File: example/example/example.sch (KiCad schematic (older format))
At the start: 9 parts, among them U1 ATMEGA32U4

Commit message: Kicad template 4x12
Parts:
- removed U1: ATMEGA32U4, mx:Pro_Micro, symbol mx:ATMEGA32U4
- added D10, D11, D12, D15, D16, D17, D18, D19, D20, D21, D22, D23, D24, D25, D26, D27, D28, D29, D3, D30, D31, D32, D33, D34, D35, D36, D37, D38, D39, D4, D40, D41, D42, D43, D44, D45, D46, D47, D48, D5, D6, D7, D8, D9: D, Diode_THT:D_DO-35_SOD27_P7.62mm_Horizontal, symbol Device:D
- added K10, K11, K12, K15, K16, K17, K18, K19, K20, K21, K22, K23, K24, K25, K26, K27, K28, K29, K3, K30, K31, K32, K33, K34, K35, K36, K37, K38, K39, K4, K40, K41, K42, K43, K44, K45, K46, K47, K48, K5, K6, K7, K8, K9: KEYSW, Button_Switch_Keyboard:SW_Cherry_MX_1.00u_Plate, symbol example-rescue:KEYSW-mx
- added SW1: SW_Push, Button_Switch_THT:SW_PUSH_6mm_H5mm, symbol Switch:SW_Push
- added U1: ProMicro, localib:pro_micro, symbol ProMicro:ProMicro
- D1: renamed from D2; footprint Diode_THT:D_DO-15_P10.16mm_Horizontal -> Diode_THT:D_DO-35_SOD27_P7.62mm_Horizontal
- D13: renamed from D1; footprint Diode_THT:D_DO-15_P10.16mm_Horizontal -> Diode_THT:D_DO-35_SOD27_P7.62mm_Horizontal
- D14: renamed from D4; footprint Diode_THT:D_DO-15_P10.16mm_Horizontal -> Diode_THT:D_DO-35_SOD27_P7.62mm_Horizontal
- D2: renamed from D3; footprint Diode_THT:D_DO-15_P10.16mm_Horizontal -> Diode_THT:D_DO-35_SOD27_P7.62mm_Horizontal
- K1: renamed from K?2; footprint Button_Switch_Keyboard:SW_Cherry_MX_1.00u_PCB -> Button_Switch_Keyboard:SW_Cherry_MX_1.00u_Plate; symbol mx:KEYSW -> example-rescue:KEYSW-mx
- K13: renamed from K?1; footprint Button_Switch_Keyboard:SW_Cherry_MX_1.00u_PCB -> Button_Switch_Keyboard:SW_Cherry_MX_1.00u_Plate; symbol mx:KEYSW -> example-rescue:KEYSW-mx
- K14: renamed from K?4; footprint Button_Switch_Keyboard:SW_Cherry_MX_1.00u_PCB -> Button_Switch_Keyboard:SW_Cherry_MX_1.00u_Plate; symbol mx:KEYSW -> example-rescue:KEYSW-mx
- K2: renamed from K?3; footprint Button_Switch_Keyboard:SW_Cherry_MX_1.00u_PCB -> Button_Switch_Keyboard:SW_Cherry_MX_1.00u_Plate; symbol mx:KEYSW -> example-rescue:KEYSW-mx
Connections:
- net +5V: now also U1.21 (5V)
- net col0: now also K25.1, K37.1, U1.20 (21)
- net col1: now also K26.1, K38.1, U1.19 (20)
- net row0: now also D1.1 (K), D2.1 (K), D10.1 (K), D11.1 (K), D12.1 (K), D3.1 (K), D4.1 (K), D5.1 (K), D6.1 (K), D7.1 (K), D8.1 (K), D9.1 (K), U1.18 (19)
- net row1: now also D13.1 (K), D14.1 (K), D15.1 (K), D16.1 (K), D17.1 (K), D18.1 (K), D19.1 (K), D20.1 (K), D21.1 (K), D22.1 (K), D23.1 (K), D24.1 (K), U1.15 (14)
- new net: SW1.1, U1.22 (RST)
- new net: D25.2 (A), K25.2
- new net: D37.2 (A), K37.2
- new net: D26.2 (A), K26.2
- new net: D38.2 (A), K38.2
- new net: D3.2 (A), K3.2
- new net: D4.2 (A), K4.2
- new net: D5.2 (A), K5.2
- new net: D6.2 (A), K6.2
- new net: D7.2 (A), K7.2
- new net: D8.2 (A), K8.2
- new net: D9.2 (A), K9.2
- new net: D10.2 (A), K10.2
- new net: D11.2 (A), K11.2
- new net: D27.2 (A), K27.2
- new net: D39.2 (A), K39.2
- new net: D16.2 (A), K16.2
- new net: D12.2 (A), K12.2
- new net: D28.2 (A), K28.2
- new net: D40.2 (A), K40.2
- new net: D29.2 (A), K29.2
- new net: D17.2 (A), K17.2
- new net: D41.2 (A), K41.2
- new net: D18.2 (A), K18.2
- new net: D19.2 (A), K19.2
- new net: D20.2 (A), K20.2
- new net: D21.2 (A), K21.2
- new net: D22.2 (A), K22.2
- new net: D23.2 (A), K23.2
- new net: D24.2 (A), K24.2
- new net: D30.2 (A), K30.2
- new net: D31.2 (A), K31.2
- new net: D32.2 (A), K32.2
- new net: D33.2 (A), K33.2
- new net: D34.2 (A), K34.2
- new net: D35.2 (A), K35.2
- new net: D36.2 (A), K36.2
- new net: D42.2 (A), K42.2
- new net: D43.2 (A), K43.2
- new net: D44.2 (A), K44.2
- new net: D45.2 (A), K45.2
- new net: D46.2 (A), K46.2
- new net: D47.2 (A), K47.2
- new net: D48.2 (A), K48.2
- new net GND: SW1.2, U1.23 (GND), U1.3 (GND), U1.4 (GND)
- new net col10: K11.1, K23.1, K35.1, K47.1, U1.2 (0)
- new net col11: K12.1, K24.1, K36.1, K48.1, U1.1
- new net col2: K15.1, K27.1, K3.1, K39.1, U1.12 (9)
- new net col3: K16.1, K28.1, K4.1, K40.1, U1.11 (8)
- new net col4: K17.1, K29.1, K41.1, K5.1, U1.10 (7)
- new net col5: K18.1, K30.1, K42.1, K6.1, U1.9 (6)
- new net col6: K19.1, K31.1, K43.1, K7.1, U1.8 (5)
- new net col7: K20.1, K32.1, K44.1, K8.1, U1.7 (4)
- new net col8: K21.1, K33.1, K45.1, K9.1, U1.6 (3)
- new net col9: K10.1, K22.1, K34.1, K46.1, U1.5 (2)
- new net pin15: U1.16 (15)
- new net pin18: U1.17 (18)
- new net row2: D25.1 (K), D26.1 (K), D27.1 (K), D28.1 (K), D29.1 (K), D30.1 (K), D31.1 (K), D32.1 (K), D33.1 (K), D34.1 (K), D35.1 (K), D36.1 (K), U1.14 (16)
- new net row3: D37.1 (K), D38.1 (K), D39.1 (K), D40.1 (K), D41.1 (K), D42.1 (K), D43.1 (K), D44.1 (K), D45.1 (K), D46.1 (K), D47.1 (K), D48.1 (K), U1.13 (10)
- no-connect marks 38 -> 1
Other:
- moved on the sheet: D1, D13, D14, D2, K1, K13, K14, K2

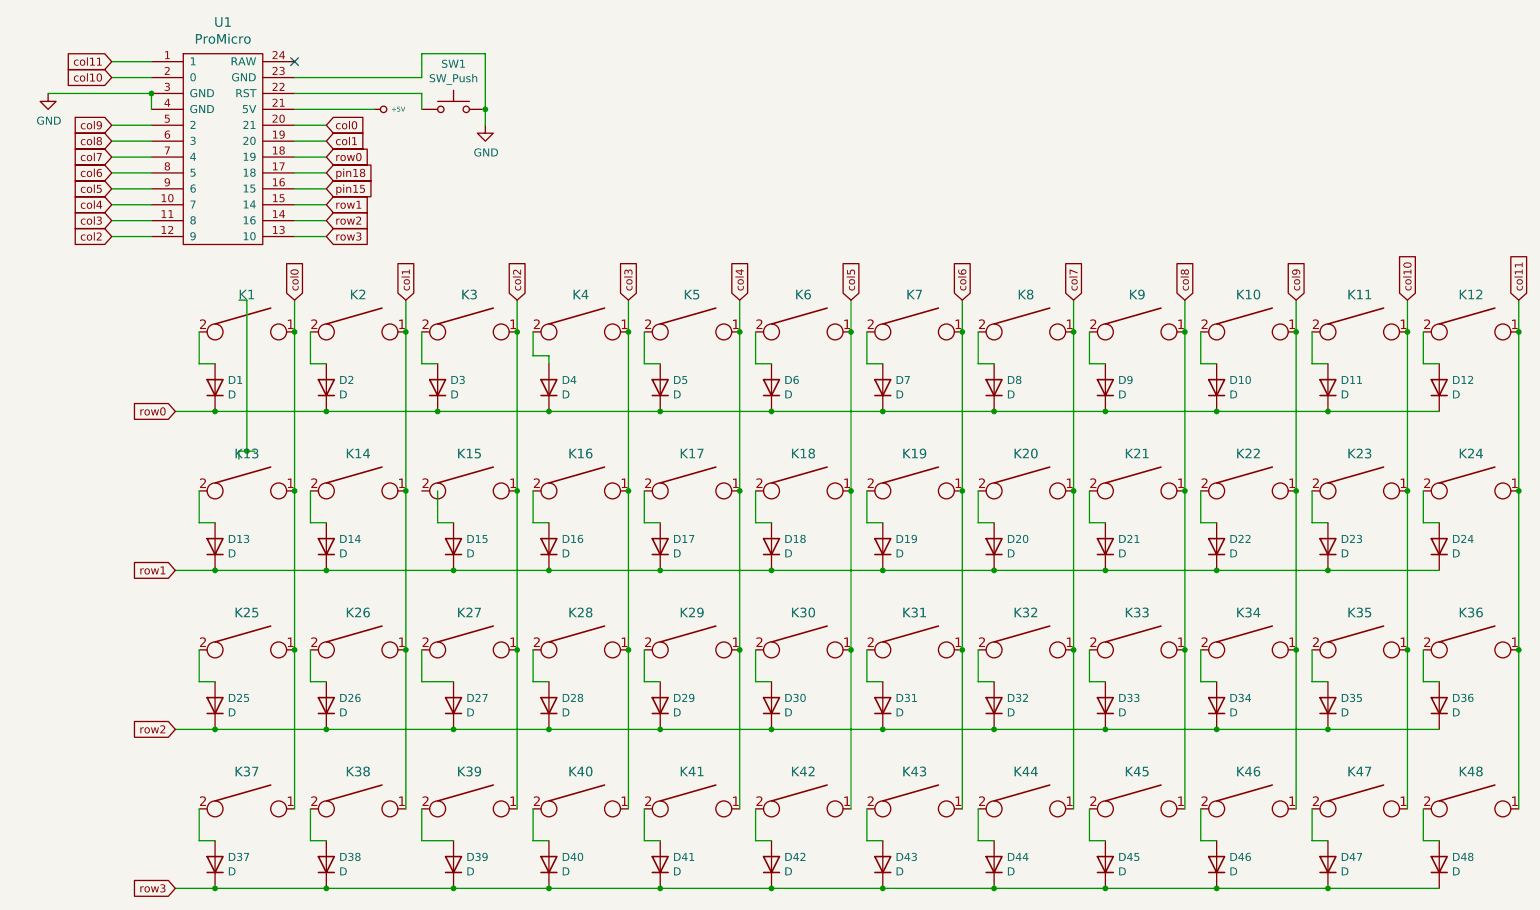
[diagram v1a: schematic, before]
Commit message: Kicad template 4x12 not wired
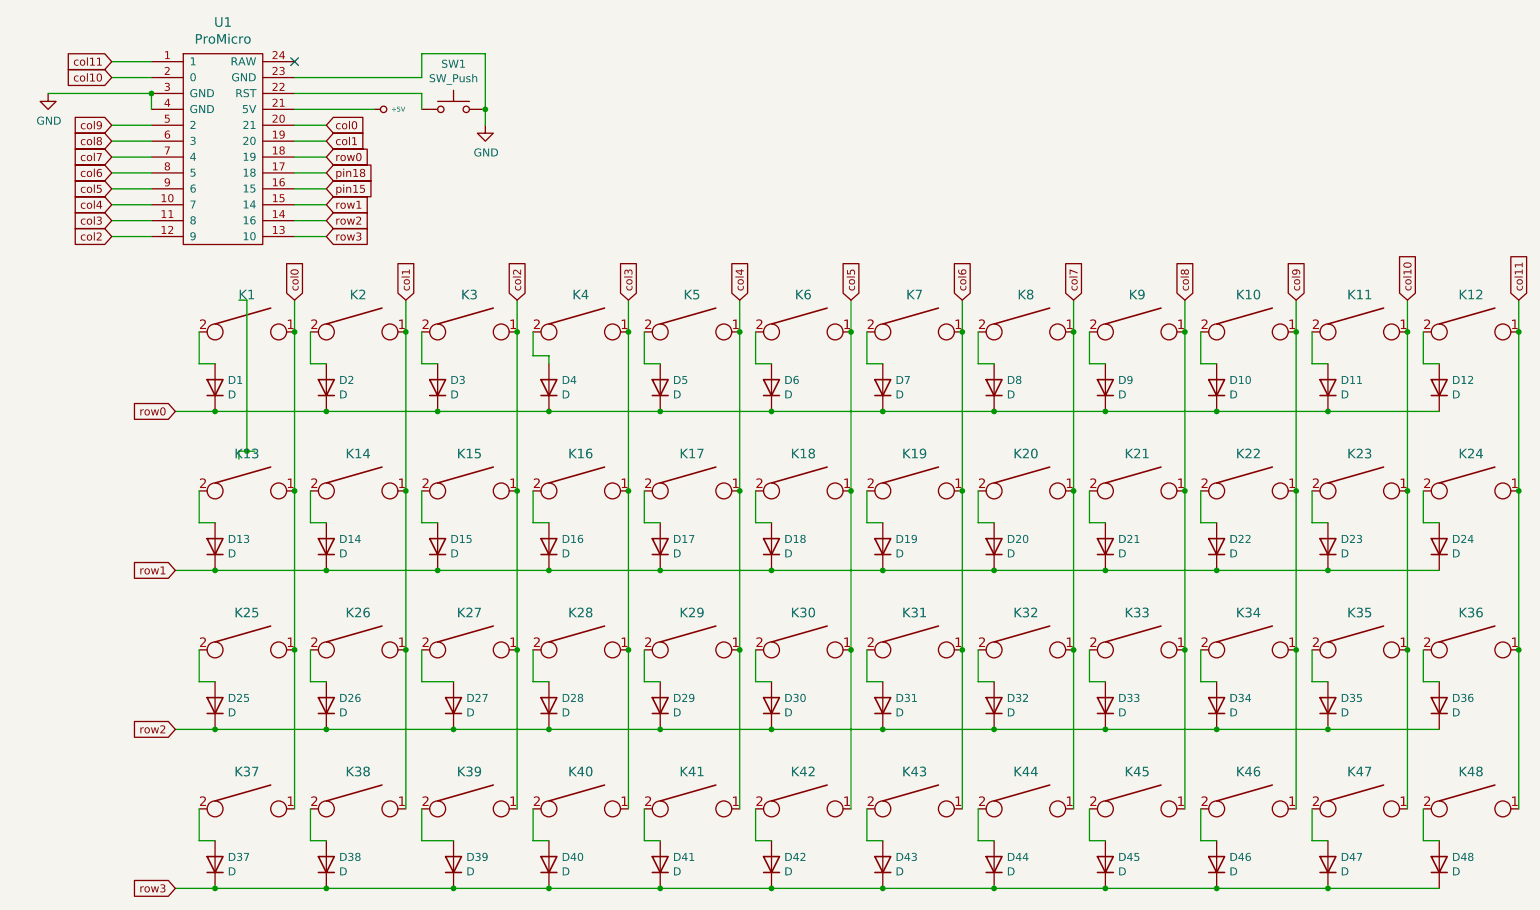
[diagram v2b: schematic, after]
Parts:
- SW1: footprint Button_Switch_THT:SW_PUSH_6mm_H5mm -> Connector_PinHeader_2.54mm:PinHeader_2x01_P2.54mm_Vertical
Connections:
- net at K15.2: now also D15.2 (A)
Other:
- moved on the sheet: D15
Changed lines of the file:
@@
 L Device:D D15
 U 1 1 5FA9556D
-P 3800 3850
-F 0 "D15" V 3846 3770 50  0000 R CNN
-F 1 "D" V 3755 3770 50  0000 R CNN
-F 2 "Diode_THT:D_DO-35_SOD27_P7.62mm_Horizontal" H 3800 3850 50  0001 C CNN
-F 3 "~" H 3800 3850 50  0001 C CNN
-	1    3800 3850
+P 3700 3850
+F 0 "D15" V 3746 3770 50  0000 R CNN
+F 1 "D" V 3655 3770 50  0000 R CNN
+F 2 "Diode_THT:D_DO-35_SOD27_P7.62mm_Horizontal" H 3700 3850 50  0001 C CNN
+F 3 "~" H 3700 3850 50  0001 C CNN
+	1    3700 3850
 	0    -1   -1   0
 $EndComp
@@
 Wire Wire Line
 	4200 4500 4200 3500
-Wire Wire Line
-	3800 4000 3000 4000
 Connection ~ 3000 4000
 Wire Wire Line
@@
 Wire Wire Line
 	4300 3700 4400 3700
-Wire Wire Line
-	4400 4000 3800 4000
-Connection ~ 3800 4000
 $Comp
 L example-rescue:KEYSW-mx K28
@@
 Wire Wire Line
 	5100 4000 4400 4000
-Connection ~ 4400 4000
 Wire Wire Line
 	5100 5000 4400 5000
@@
 	0    -1   -1   0
 $EndComp
-$Comp
-L Device:D D48
-U 1 1 5FB45D79
-P 10000 5850
-F 0 "D48" V 10046 5770 50  0000 R CNN
-F 1 "D" V 9955 5770 50  0000 R CNN
-F 2 "Diode_THT:D_DO-35_SOD27_P7.62mm_Horizontal" H 10000 5850 50  0001 C CNN
-F 3 "~" H 10000 5850 50  0001 C CNN
-	1    10000 5850
-	0    -1   -1   0
-$EndComp
 Wire Wire Line
 	7000 4500 7000 5500
@@
 	10000 6000 9300 6000
 Connection ~ 9300 6000
-Wire Wire Line
-	10000 5700 9900 5700
-Wire Wire Line
-	9900 5700 9900 5500
 Wire Wire Line
 	9300 5700 9200 5700
@@
 F 0 "SW1" H 3800 1385 50  0000 C CNN
 F 1 "SW_Push" H 3800 1294 50  0000 C CNN
-F 2 "Button_Switch_THT:SW_PUSH_6mm_H5mm" H 3800 1300 50  0001 C CNN
+F 2 "Connector_PinHeader_2.54mm:PinHeader_2x01_P2.54mm_Vertical" H 3800 1300 50  0001 C CNN
 F 3 "~" H 3800 1300 50  0001 C CNN
 	1    3800 1100
@@
 	2900 5700 2900 5500
 Wire Wire Line
-	3800 3700 3700 3700
-Wire Wire Line
-	3700 3700 3700 3500
-Wire Wire Line
 	10000 3700 9900 3700
 Wire Wire Line
@@
 	6300 4500 6300 5500
 Connection ~ 6300 4500
+Wire Wire Line
+	3700 4000 3000 4000
+Wire Wire Line
+	4400 4000 3700 4000
+Connection ~ 4400 4000
+Connection ~ 3700 4000
+Wire Wire Line
+	3700 3700 3600 3700
+Wire Wire Line
+	3600 3700 3600 3500
+$Comp
+L Device:D D48
+U 1 1 5FB45D79
+P 10000 5850
+F 0 "D48" V 10046 5770 50  0000 R CNN
+F 1 "D" V 9955 5770 50  0000 R CNN
+F 2 "Diode_THT:D_DO-35_SOD27_P7.62mm_Horizontal" H 10000 5850 50  0001 C CNN
+F 3 "~" H 10000 5850 50  0001 C CNN
+	1    10000 5850
+	0    -1   -1   0
+$EndComp
+Wire Wire Line
+	9900 5500 9900 5700
+Wire Wire Line
+	9900 5700 10000 5700
 $EndSCHEMATC
